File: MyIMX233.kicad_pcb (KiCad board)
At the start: 2 copper layers, 74.1 x 92 mm, 82 parts, among them IC1 iMX233, IC2 DDR_SDRAM_MT46_x16, J1 USB_OTG, P1 P4v2, P2 1v2, P3 VDDA1v8, P4 2v5, P5 3v3, P6 P4v2, SW1 SWITCH_PUSHBUTTON, Y1 24Mhz

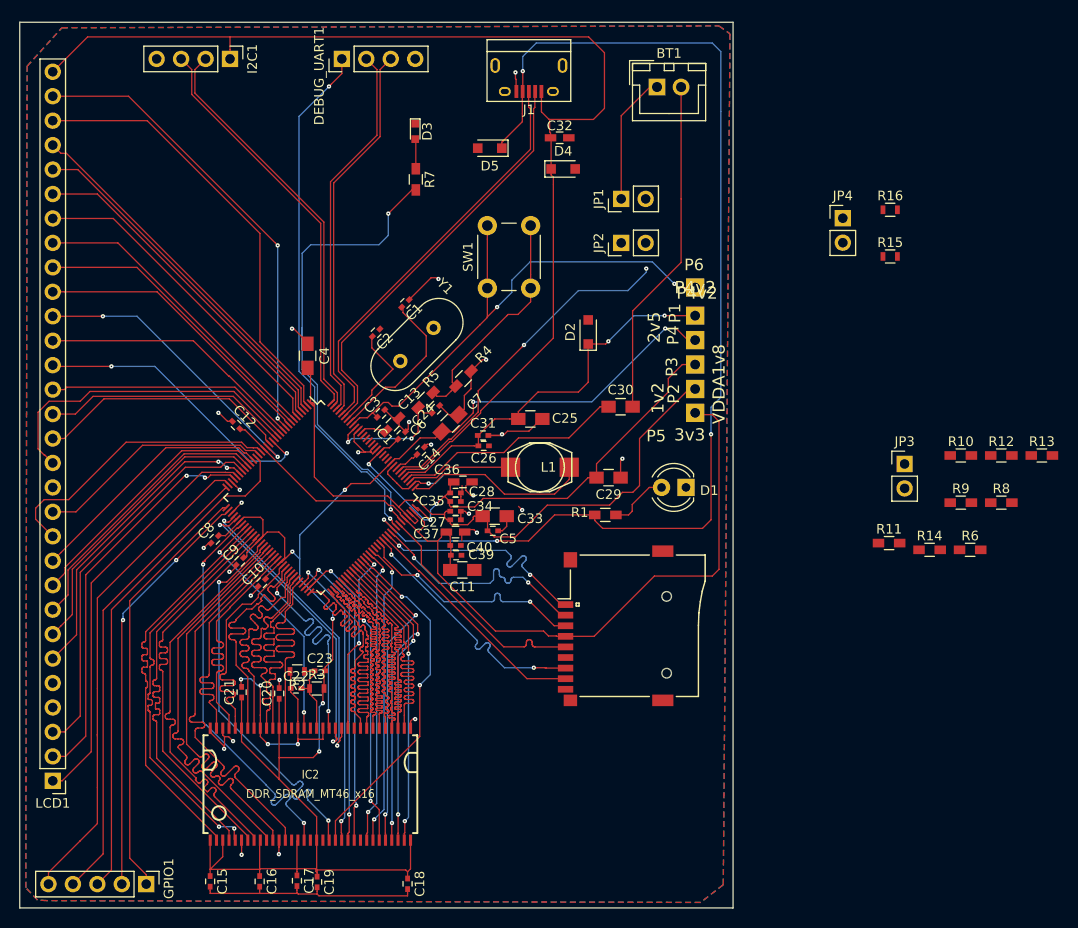
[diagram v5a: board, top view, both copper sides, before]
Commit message: resistors placement
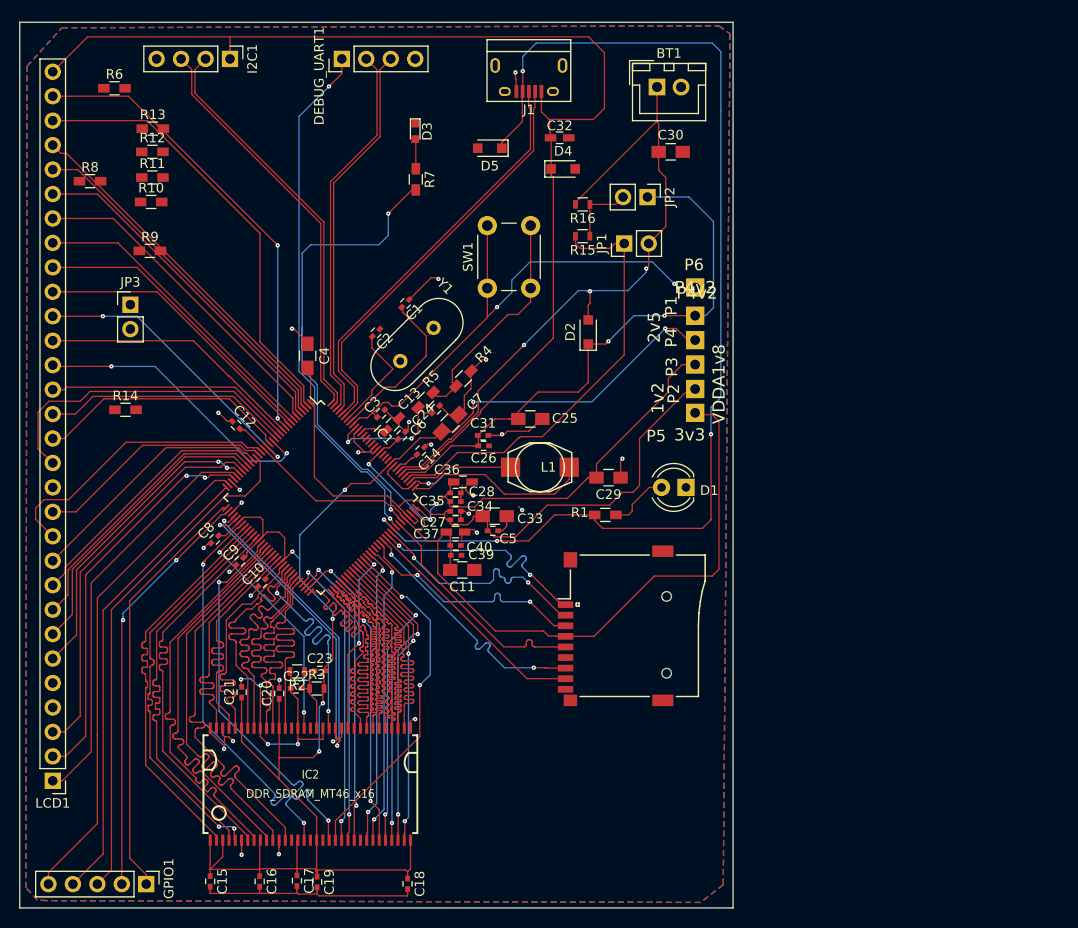
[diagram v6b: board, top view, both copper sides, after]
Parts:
- removed JP4: WithBatt, Pin_Headers:Pin_Header_Straight_1x02_Pitch2.54mm
- JP1: value Jumper -> WithBatt
- moved R6 101.0 mm to (75.6, 56.4)
- moved R8 100.4 mm to (73.0, 66.0)
- moved R13 98.4 mm to (79.5, 60.6)
- moved R12 93.7 mm to (79.5, 63.0)
- moved R9 88.2 mm to (79.2, 73.3)
- moved R10 88.1 mm to (79.4, 68.2)
- moved R11 85.4 mm to (79.5, 65.7)
- moved R14 84.8 mm to (76.7, 89.8)
- moved JP3 82.1 mm to (77.2, 78.9)
- moved R15 32.0 mm to (124.2, 71.8), turned to 180 degrees
- moved R16 31.9 mm to (124.2, 68.5), turned to 180 degrees
- moved C30 27.0 mm to (133.3, 63.0)
- moved JP2 5.49 mm to (130.9, 67.7), turned to 270 degrees
- moved JP1 4.65 mm to (128.5, 72.5)
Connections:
- net Net-(C25-Pad2) renamed /DCDC_4P2
- C15 pad 1: 2V5_VDDM -> 2V5_SYS
- C16 pad 1: 2V5_VDDM -> 2V5_SYS
- C17 pad 1: 2V5_VDDM -> 2V5_SYS
- C18 pad 1: 2V5_VDDM -> 2V5_SYS
- C19 pad 1: 2V5_VDDM -> 2V5_SYS
- C20 pad 1: 2V5_VDDM -> 2V5_SYS
- C21 pad 1: 2V5_VDDM -> 2V5_SYS
- C23 pad 2: 2V5_VDDM -> 2V5_SYS
- C30 pad 2: Net-(C30-Pad2) -> GND
- IC1 pad 100: Net-(IC1-Pad100) -> /DCDC_BATT
- IC2 pad 1: 2V5_VDDM -> 2V5_SYS
- IC2 pad 15: 2V5_VDDM -> 2V5_SYS
- IC2 pad 18: 2V5_VDDM -> 2V5_SYS
- IC2 pad 3: 2V5_VDDM -> 2V5_SYS
- IC2 pad 33: 2V5_VDDM -> 2V5_SYS
- IC2 pad 55: 2V5_VDDM -> 2V5_SYS
- IC2 pad 61: 2V5_VDDM -> 2V5_SYS
- IC2 pad 9: 2V5_VDDM -> 2V5_SYS
- J1 pad 6: Net-(J1-Pad6) -> GND
- JP1 pad 1: 2V5_SYS -> /DCDC_BATT
- JP1 pad 2: 2V5_VDDM -> /+VE
- R15 pad 2: Net-(IC1-Pad100) -> /DCDC_BATT
- R3 pad 2: 2V5_VDDM -> 2V5_SYS
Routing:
- net /DCDC_BATT: track 0.00 -> 45.7 mm
- net GND: track 161.3 -> 126.0 mm
- net /DCDC_4P2: track 40.5 -> 59.7 mm
- net Net-(JP2-Pad2): track 0.09 -> 7.06 mm
- net /+VE: track 73.5 -> 72.4 mm, vias 2 -> 3

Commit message: boot resistors added
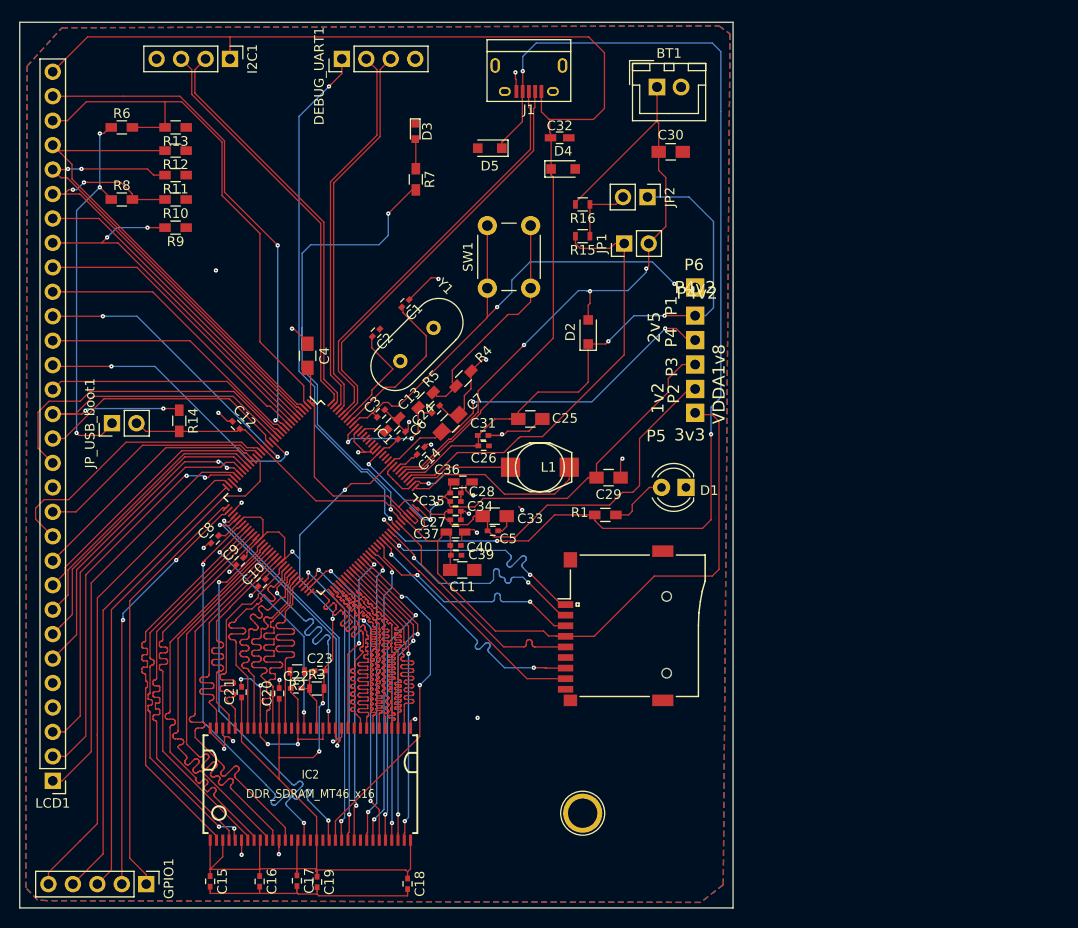
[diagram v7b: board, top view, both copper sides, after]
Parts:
- removed JP3: USB_boot, Pin_Headers:Pin_Header_Straight_1x02_Pitch2.54mm
- added JP_USB_boot1: USB_boot, Pin_Headers:Pin_Header_Straight_1x02_Pitch2.54mm, F.Cu at (75.3, 91.2)
- added REF**: 1pin, Connectors:1pin, F.Cu at (124.2, 131.7)
- moved R14 5.70 mm to (82.3, 90.9), turned to 270 degrees
- moved R6 4.13 mm to (76.3, 60.5)
- moved R8 3.81 mm to (76.3, 67.9)
- moved R9 3.60 mm to (81.9, 70.9), turned to 180 degrees
- moved R10 2.55 mm to (81.9, 67.9), turned to 180 degrees
- moved R11 2.43 mm to (81.9, 65.4), turned to 180 degrees
- moved R12 2.42 mm to (81.9, 62.9), turned to 180 degrees
- moved R13 2.37 mm to (81.9, 60.5), turned to 180 degrees
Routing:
- net Net-(JP_USB_boot1-Pad1): track 0.00 -> 39.9 mm, vias 0 -> 3
- net /LCD_RS: track 25.7 -> 39.1 mm, vias 0 -> 2
- net /LCD1: track 38.5 -> 50.3 mm
- net 3v3_SYS: track 90.7 -> 102.1 mm
- net /LCD3: track 36.2 -> 47.3 mm, vias 0 -> 2
- net /LCD0: track 46.3 -> 57.3 mm
- net /LCD2: track 37.4 -> 48.3 mm, vias 0 -> 2
- net /LCD5: track 32.7 -> 39.9 mm, vias 0 -> 2
- net Net-(IC1-Pad10): track 49.1 -> 52.7 mm
- net /LCD4: track 34.8 -> 33.9 mm
- net GND: vias 30 -> 32

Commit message: re routed because of pad length extention to 2mm. Generated gerver files too
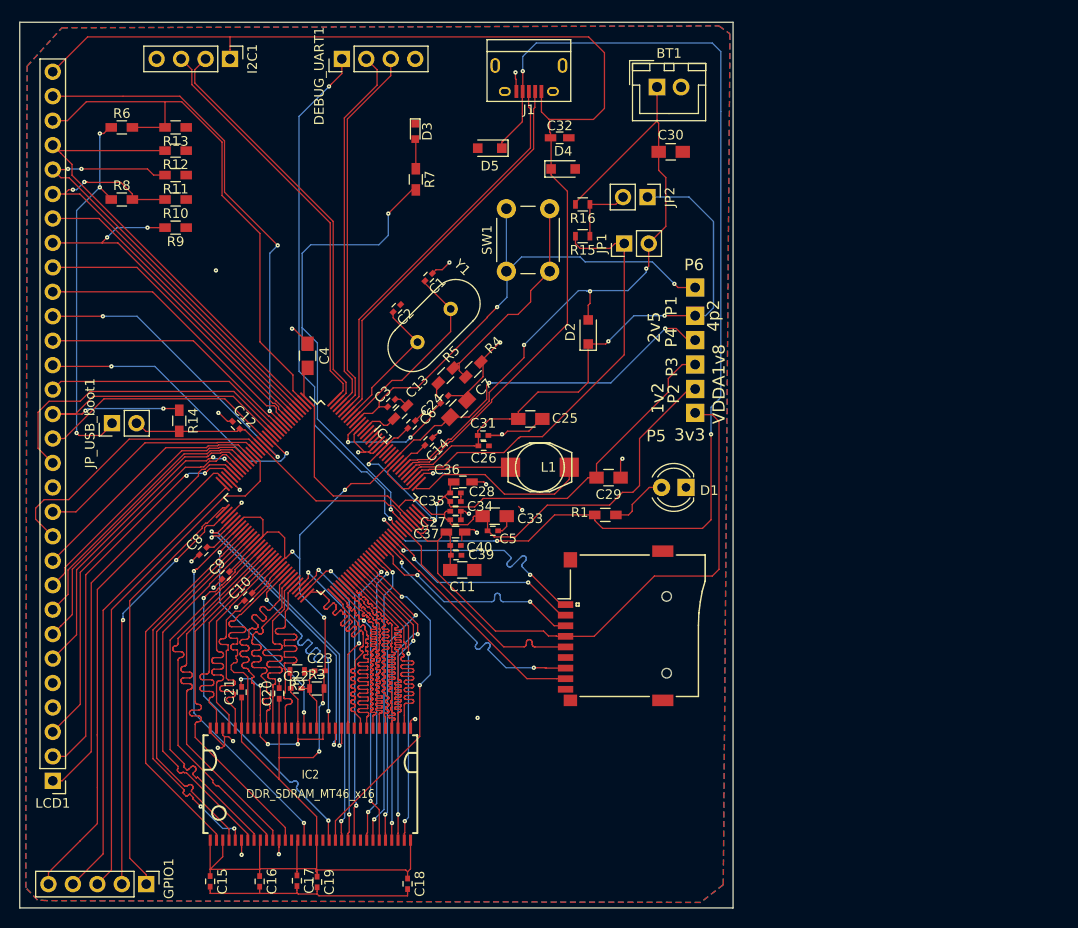
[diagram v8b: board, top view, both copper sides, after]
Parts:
- removed REF**: 1pin, Connectors:1pin
- IC1: footprint Housings_QFP:LQFP-128_14x14mm_Pitch0.4mm -> mylib:LQFP-128_14x14mm_Pitch0.4mm
- P1: value P4v2 -> 4p2
- P6: value P4v2 -> 1v
- moved C1 3.64 mm to (108.2, 76.0)
- moved C2 3.33 mm to (104.9, 79.2)
- moved R5 3.29 mm to (110.0, 86.2)
- moved Y1 2.65 mm to (110.5, 79.3)
- moved SW1 2.64 mm to (116.3, 75.4)
- moved C9 2.07 mm to (87.1, 107.0)
- moved C10 2.02 mm to (89.5, 109.2)
- moved C7 1.76 mm to (111.3, 89.7)
- moved C8 1.71 mm to (84.8, 104.5)
- moved C6 1.53 mm to (106.4, 91.3)
- moved C3 1.53 mm to (104.3, 89.1)
- moved C13 1.51 mm to (105.3, 90.0)
- moved R4 1.39 mm to (112.8, 85.6)
- moved C24 1.36 mm to (109.9, 88.7)
- moved C14 1.26 mm to (108.2, 93.1)
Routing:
- net 2V5_SYS: track 171.6 -> 176.1 mm
- net Net-(C1-Pad2): track 16.7 -> 20.8 mm
- net Net-(C2-Pad2): track 11.4 -> 15.2 mm
- net GND: track 126.0 -> 122.6 mm
- net /SD3: track 24.7 -> 21.4 mm
- net /A9: track 28.3 -> 25.6 mm
- net /D6: track 43.5 -> 40.9 mm
- net /D7: track 42.3 -> 39.7 mm
- net /D1: track 42.3 -> 39.7 mm
- net /D5: track 42.2 -> 39.6 mm
- net /D3: track 42.2 -> 39.6 mm
- net Net-(C24-Pad2): track 13.8 -> 16.3 mm
- net /D0: track 42.2 -> 39.7 mm
- net /LDQS: track 42.2 -> 39.7 mm
- net /LDM: track 42.2 -> 39.7 mm
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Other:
- rule pad_to_mask_clearance: 0 -> 0.06
